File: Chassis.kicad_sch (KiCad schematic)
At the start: 4 parts

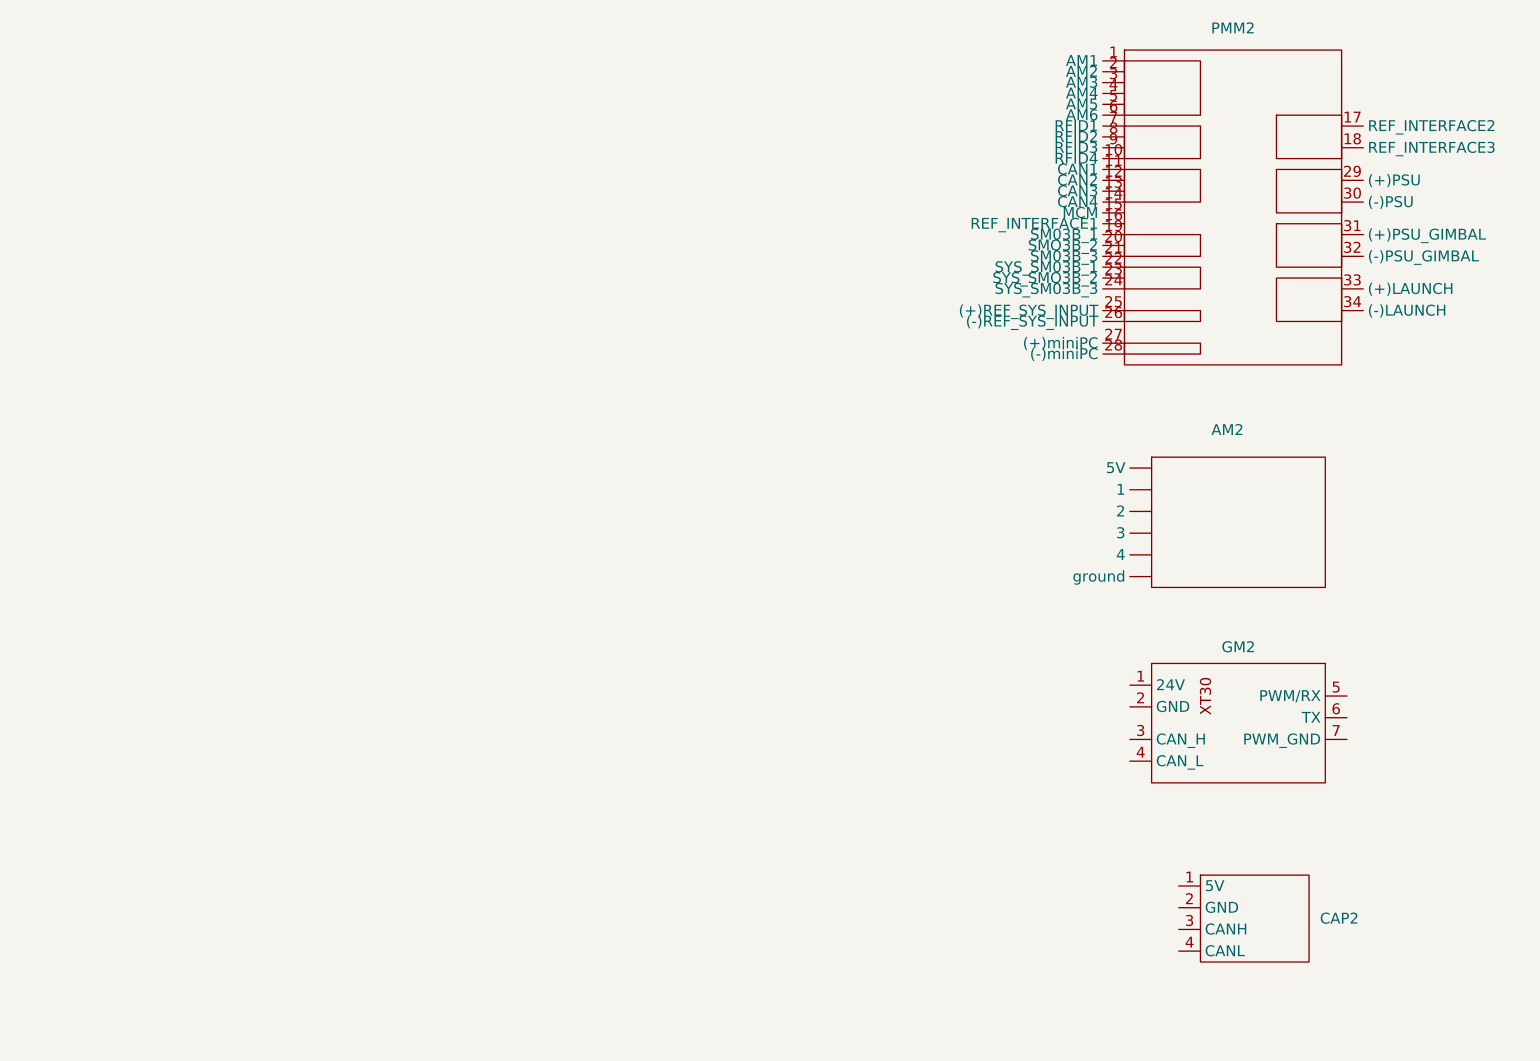
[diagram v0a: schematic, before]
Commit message: Added all connectors + assigned footprints + created PCB file
Starting layout now
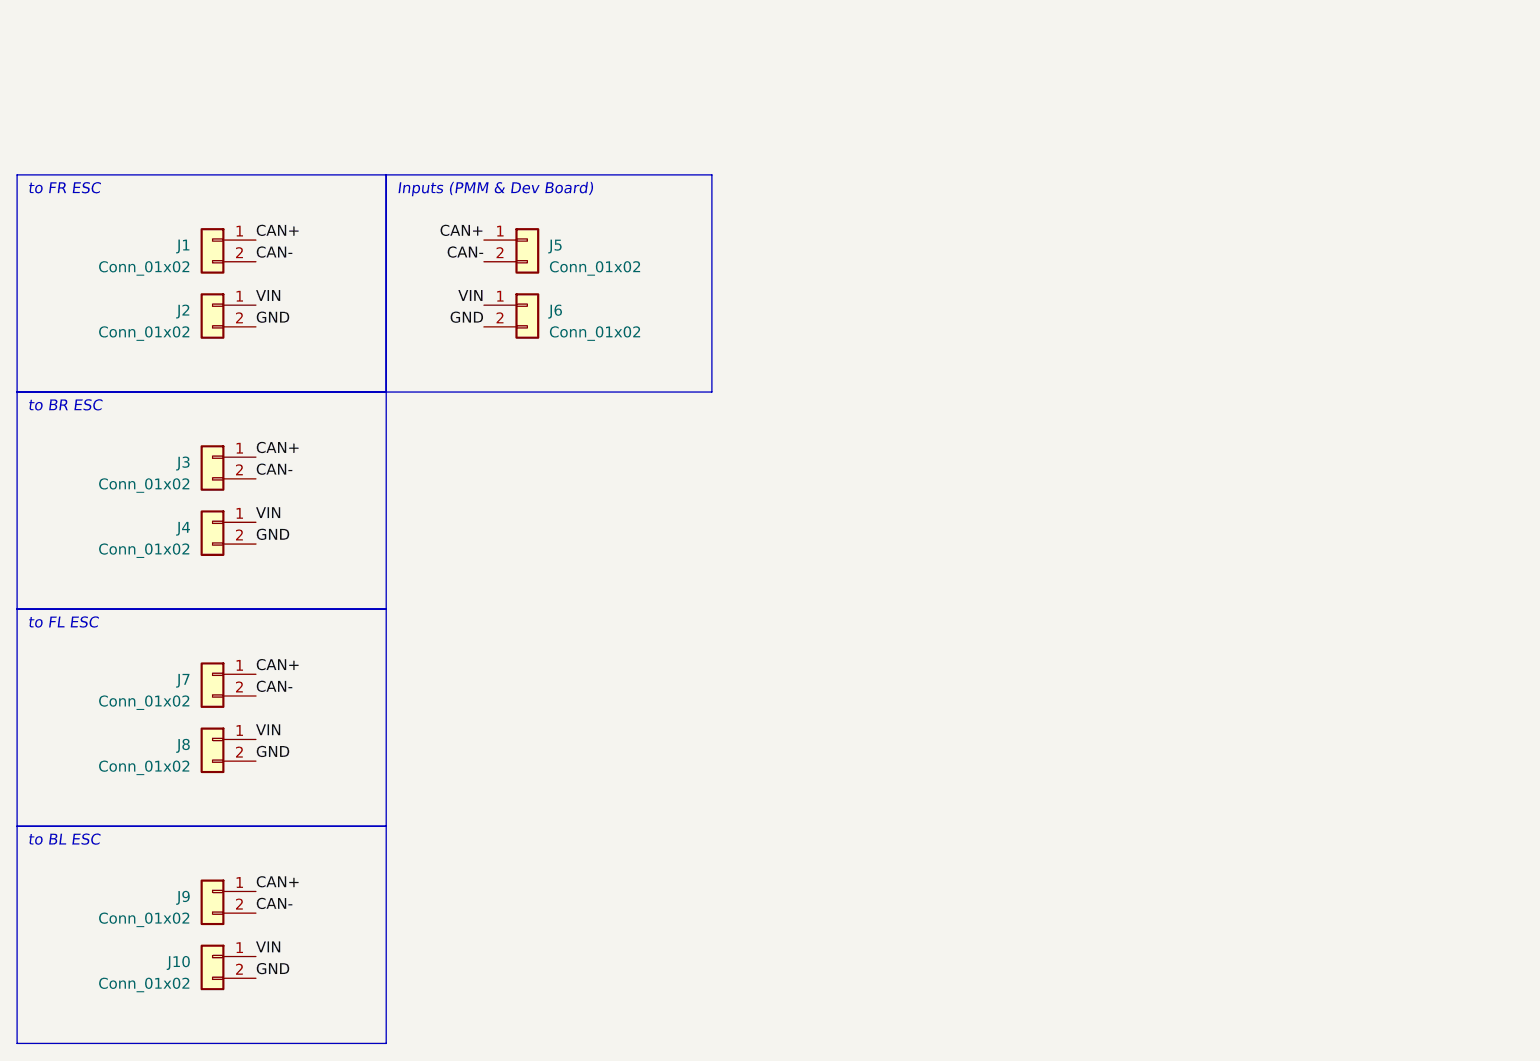
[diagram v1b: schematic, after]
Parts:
- removed AM2: ~, symbol Robomaster_Library:AM
- removed CAP2: ~, symbol Robomaster_Library:CAP
- removed GM2: ~, symbol Robomaster_Library:GM6020
- removed PMM2: ~, symbol Robomaster_Library:PMM
- added J1, J3, J5, J7, J9: Conn_01x02, Connector_JST:JST_GH_BM02B-GHS-TBT_1x02-1MP_P1.25mm_Vertical, symbol Connector_Generic:Conn_01x02
- added J10, J2, J4, J8: Conn_01x02, Connector_AMASS:AMASS_XT30U-F_1x02_P5.0mm_Vertical, symbol Connector_Generic:Conn_01x02
- added J6: Conn_01x02, Connector_AMASS:AMASS_XT60-F_1x02_P7.20mm_Vertical, symbol Connector_Generic:Conn_01x02
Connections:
- new net CAN+: J1.1 (Pin_1), J3.1 (Pin_1), J5.1 (Pin_1), J7.1 (Pin_1), J9.1 (Pin_1)
- new net CAN-: J1.2 (Pin_2), J3.2 (Pin_2), J5.2 (Pin_2), J7.2 (Pin_2), J9.2 (Pin_2)
- new net GND: J10.2 (Pin_2), J2.2 (Pin_2), J4.2 (Pin_2), J6.2 (Pin_2), J8.2 (Pin_2)
- new net VIN: J10.1 (Pin_1), J2.1 (Pin_1), J4.1 (Pin_1), J6.1 (Pin_1), J8.1 (Pin_1)
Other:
- note added: "Inputs (PMM & Dev Board)"
- note added: "to BL ESC"
- note added: "to BR ESC"
- note added: "to FL ESC"
- note added: "to FR ESC"

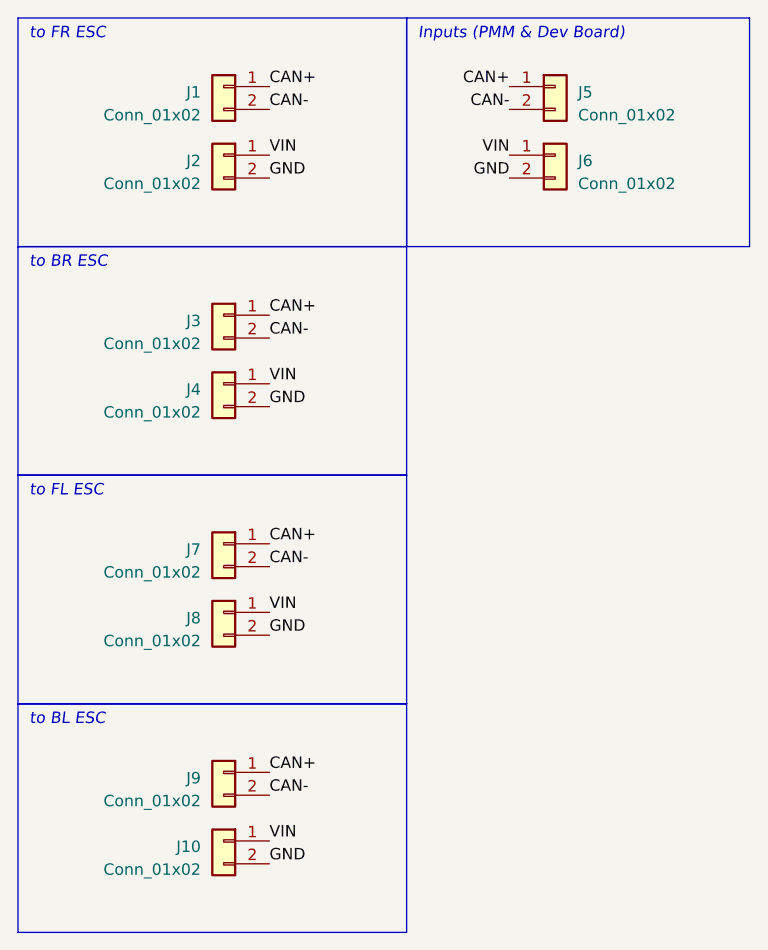
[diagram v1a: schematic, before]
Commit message: Change polarity of pins + add circular trace
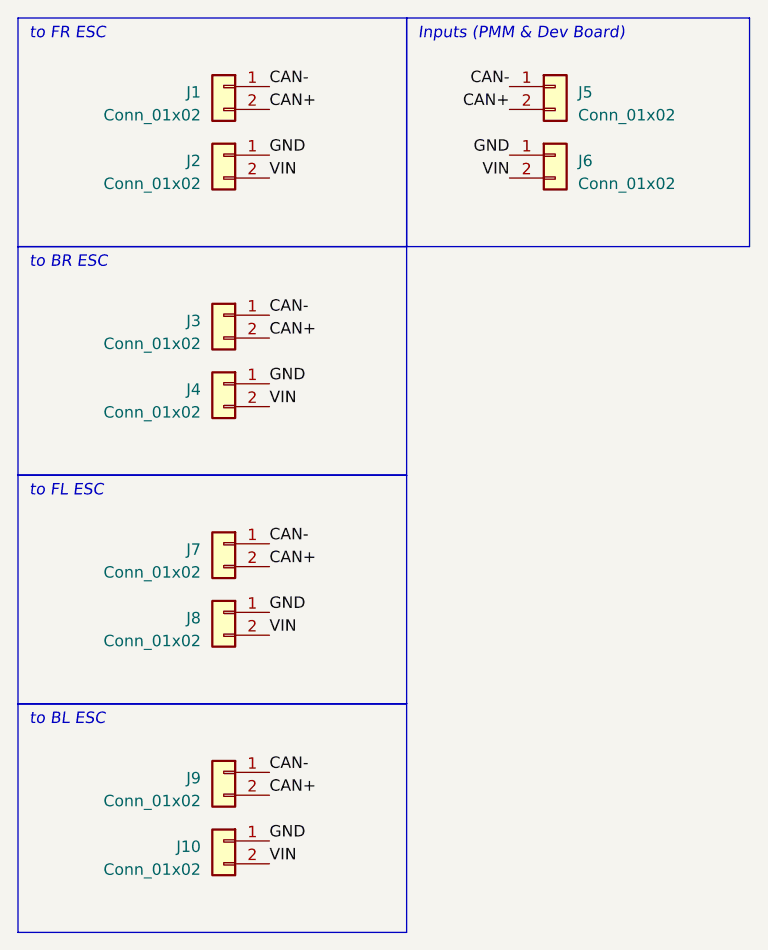
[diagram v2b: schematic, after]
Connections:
- net CAN+: now also J1.2 (Pin_2), J3.2 (Pin_2), J5.2 (Pin_2), J7.2 (Pin_2), J9.2 (Pin_2); no longer J1.1 (Pin_1), J3.1 (Pin_1), J5.1 (Pin_1), J7.1 (Pin_1), J9.1 (Pin_1)
- net CAN-: now also J1.1 (Pin_1), J3.1 (Pin_1), J5.1 (Pin_1), J7.1 (Pin_1), J9.1 (Pin_1); no longer J1.2 (Pin_2), J3.2 (Pin_2), J5.2 (Pin_2), J7.2 (Pin_2), J9.2 (Pin_2)
- net GND: now also J10.1 (Pin_1), J2.1 (Pin_1), J4.1 (Pin_1), J6.1 (Pin_1), J8.1 (Pin_1); no longer J10.2 (Pin_2), J2.2 (Pin_2), J4.2 (Pin_2), J6.2 (Pin_2), J8.2 (Pin_2)
- net VIN: now also J10.2 (Pin_2), J2.2 (Pin_2), J4.2 (Pin_2), J6.2 (Pin_2), J8.2 (Pin_2); no longer J10.1 (Pin_1), J2.1 (Pin_1), J4.1 (Pin_1), J6.1 (Pin_1), J8.1 (Pin_1)
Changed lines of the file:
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@@
     (effects (font (size 1.27 1.27) italic) (justify left bottom))
   )
-  (label "CAN-" (at 133.35 118.11 0) (fields_autoplaced)
+  (label "CAN-" (at 133.35 140.97 0) (fields_autoplaced)
     (effects (font (size 1.27 1.27)) (justify left bottom))
   )
-  (label "VIN" (at 133.35 148.59 0) (fields_autoplaced)
+  (label "GND" (at 160.02 72.39 180) (fields_autoplaced)
+    (effects (font (size 1.27 1.27)) (justify right bottom))
+  )
+  (label "CAN-" (at 133.35 115.57 0) (fields_autoplaced)
     (effects (font (size 1.27 1.27)) (justify left bottom))
   )
-  (label "CAN-" (at 133.35 67.31 0) (fields_autoplaced)
+  (label "CAN+" (at 133.35 118.11 0) (fields_autoplaced)
     (effects (font (size 1.27 1.27)) (justify left bottom))
   )
-  (label "CAN-" (at 133.35 143.51 0) (fields_autoplaced)
+  (label "CAN+" (at 133.35 143.51 0) (fields_autoplaced)
     (effects (font (size 1.27 1.27)) (justify left bottom))
   )
-  (label "VIN" (at 133.35 123.19 0) (fields_autoplaced)
+  (label "CAN-" (at 133.35 90.17 0) (fields_autoplaced)
     (effects (font (size 1.27 1.27)) (justify left bottom))
   )
-  (label "CAN+" (at 160.02 64.77 180) (fields_autoplaced)
+  (label "VIN" (at 133.35 100.33 0) (fields_autoplaced)
+    (effects (font (size 1.27 1.27)) (justify left bottom))
+  )
+  (label "GND" (at 133.35 72.39 0) (fields_autoplaced)
+    (effects (font (size 1.27 1.27)) (justify left bottom))
+  )
+  (label "VIN" (at 133.35 151.13 0) (fields_autoplaced)
+    (effects (font (size 1.27 1.27)) (justify left bottom))
+  )
+  (label "CAN+" (at 133.35 92.71 0) (fields_autoplaced)
+    (effects (font (size 1.27 1.27)) (justify left bottom))
+  )
+  (label "VIN" (at 133.35 125.73 0) (fields_autoplaced)
+    (effects (font (size 1.27 1.27)) (justify left bottom))
+  )
+  (label "VIN" (at 133.35 74.93 0) (fields_autoplaced)
+    (effects (font (size 1.27 1.27)) (justify left bottom))
+  )
+  (label "CAN-" (at 133.35 64.77 0) (fields_autoplaced)
+    (effects (font (size 1.27 1.27)) (justify left bottom))
+  )
+  (label "GND" (at 133.35 123.19 0) (fields_autoplaced)
+    (effects (font (size 1.27 1.27)) (justify left bottom))
+  )
+  (label "CAN+" (at 160.02 67.31 180) (fields_autoplaced)
     (effects (font (size 1.27 1.27)) (justify right bottom))
   )
-  (label "VIN" (at 160.02 72.39 180) (fields_autoplaced)
+  (label "GND" (at 133.35 148.59 0) (fields_autoplaced)
+    (effects (font (size 1.27 1.27)) (justify left bottom))
+  )
+  (label "CAN+" (at 133.35 67.31 0) (fields_autoplaced)
+    (effects (font (size 1.27 1.27)) (justify left bottom))
+  )
+  (label "VIN" (at 160.02 74.93 180) (fields_autoplaced)
     (effects (font (size 1.27 1.27)) (justify right bottom))
   )
-  (label "CAN+" (at 133.35 64.77 0) (fields_autoplaced)
+  (label "GND" (at 133.35 97.79 0) (fields_autoplaced)
     (effects (font (size 1.27 1.27)) (justify left bottom))
   )
-  (label "GND" (at 133.35 74.93 0) (fields_autoplaced)
-    (effects (font (size 1.27 1.27)) (justify left bottom))
-  )
-  (label "VIN" (at 133.35 97.79 0) (fields_autoplaced)
-    (effects (font (size 1.27 1.27)) (justify left bottom))
-  )
-  (label "GND" (at 133.35 151.13 0) (fields_autoplaced)
-    (effects (font (size 1.27 1.27)) (justify left bottom))
-  )
-  (label "CAN+" (at 133.35 115.57 0) (fields_autoplaced)
-    (effects (font (size 1.27 1.27)) (justify left bottom))
-  )
-  (label "CAN-" (at 160.02 67.31 180) (fields_autoplaced)
+  (label "CAN-" (at 160.02 64.77 180) (fields_autoplaced)
     (effects (font (size 1.27 1.27)) (justify right bottom))
   )
-  (label "CAN+" (at 133.35 140.97 0) (fields_autoplaced)
-    (effects (font (size 1.27 1.27)) (justify left bottom))
-  )
-  (label "VIN" (at 133.35 72.39 0) (fields_autoplaced)
-    (effects (font (size 1.27 1.27)) (justify left bottom))
-  )
-  (label "CAN-" (at 133.35 92.71 0) (fields_autoplaced)
-    (effects (font (size 1.27 1.27)) (justify left bottom))
-  )
-  (label "GND" (at 133.35 100.33 0) (fields_autoplaced)
-    (effects (font (size 1.27 1.27)) (justify left bottom))
-  )
-  (label "CAN+" (at 133.35 90.17 0) (fields_autoplaced)
-    (effects (font (size 1.27 1.27)) (justify left bottom))
-  )
-  (label "GND" (at 133.35 125.73 0) (fields_autoplaced)
-    (effects (font (size 1.27 1.27)) (justify left bottom))
-  )
-  (label "GND" (at 160.02 74.93 180) (fields_autoplaced)
-    (effects (font (size 1.27 1.27)) (justify right bottom))
-  )

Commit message: Possible indicator method?
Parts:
- added D1: LED, symbol Device:LED
- added Q1: NMOS, symbol Simulation_SPICE:NMOS
- added R2: REF_R, Resistor_SMD:R_0603_1608Metric_Pad0.98x0.95mm_HandSolder, symbol Device:R_US
- added R3: PUR, Resistor_SMD:R_0603_1608Metric_Pad0.98x0.95mm_HandSolder, symbol Device:R_US
- added TP1, TP2, TP3: TestPoint, TestPoint:TestPoint_Pad_1.0x1.0mm, symbol Connector:TestPoint
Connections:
- net CAN+: now also Q1.2 (G), TP2.1
- net CAN-: now also TP1.1
- net GND: now also R3.2, TP3.1
- net VIN: now also D1.2 (A), R2.1
- new net: D1.1 (K), Q1.1 (D)
- new net VREF: Q1.3 (S), R2.2, R3.1
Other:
- note added: "CAN Indicator Light"
- note added: "Test points"
- moved on the sheet: J5, J6

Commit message: Lakshay's method
I disagree
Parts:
- removed Q1: NMOS, symbol Simulation_SPICE:NMOS
- removed R2: REF_R, Resistor_SMD:R_0603_1608Metric_Pad0.98x0.95mm_HandSolder, symbol Device:R_US
- removed R3: PUR, Resistor_SMD:R_0603_1608Metric_Pad0.98x0.95mm_HandSolder, symbol Device:R_US
- added R1: UR, Resistor_SMD:R_0603_1608Metric_Pad0.98x0.95mm_HandSolder, symbol Device:R_US
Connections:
- net CAN+: now also D1.2 (A)
- net GND: now also R1.1
- net VIN: no longer D1.2 (A)
- net at D1.1 (K): now also R1.2
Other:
- note added: "Lakshay says yes I say no"

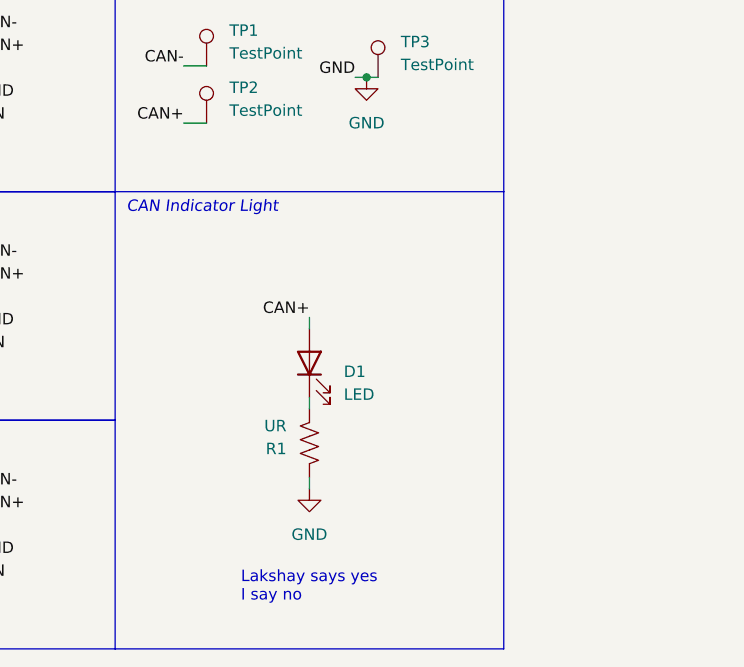
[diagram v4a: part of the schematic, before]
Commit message: Change to MOSFET architecture
Low-side switching ftw
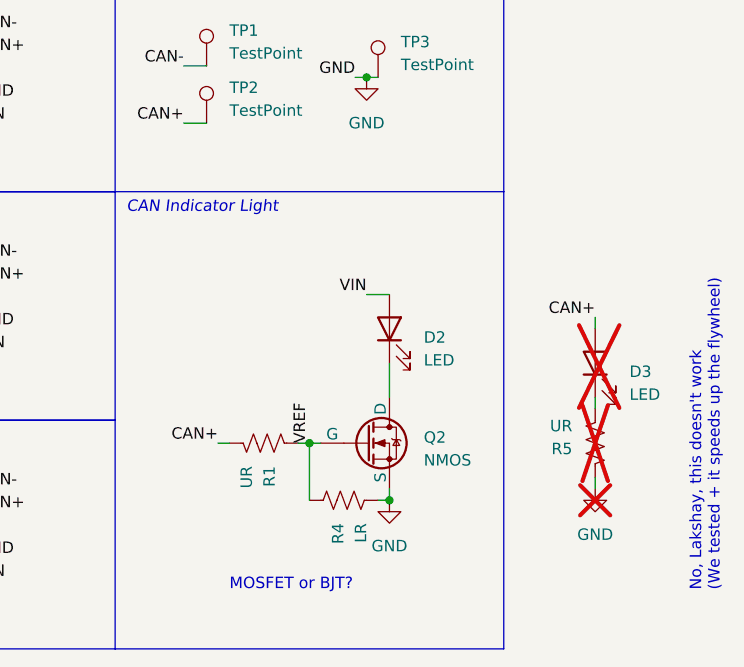
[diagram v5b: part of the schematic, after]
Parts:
- removed D1: LED, symbol Device:LED
- added D2, D3: LED, symbol Device:LED
- added Q2: NMOS, symbol Simulation_SPICE:NMOS
- added R4: LR, Resistor_SMD:R_0603_1608Metric_Pad0.98x0.95mm_HandSolder, symbol Device:R_US
- added R5: UR, Resistor_SMD:R_0603_1608Metric_Pad0.98x0.95mm_HandSolder, symbol Device:R_US
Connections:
- net CAN+: now also R1.2, D3.2 (A)
- net GND: now also Q2.3 (S), R4.2, R5.1; no longer R1.1
- net VIN: now also D2.2 (A)
- new net: D3.1 (K), R5.2
- new net: D2.1 (K), Q2.1 (D)
- new net VREF: Q2.2 (G), R1.1, R4.1
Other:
- note added: "MOSFET or BJT?"
- note added: "No, Lakshay, this doesn't work (We tested + it speeds up the flywheel)"
- note removed: "Lakshay says yes I say no"

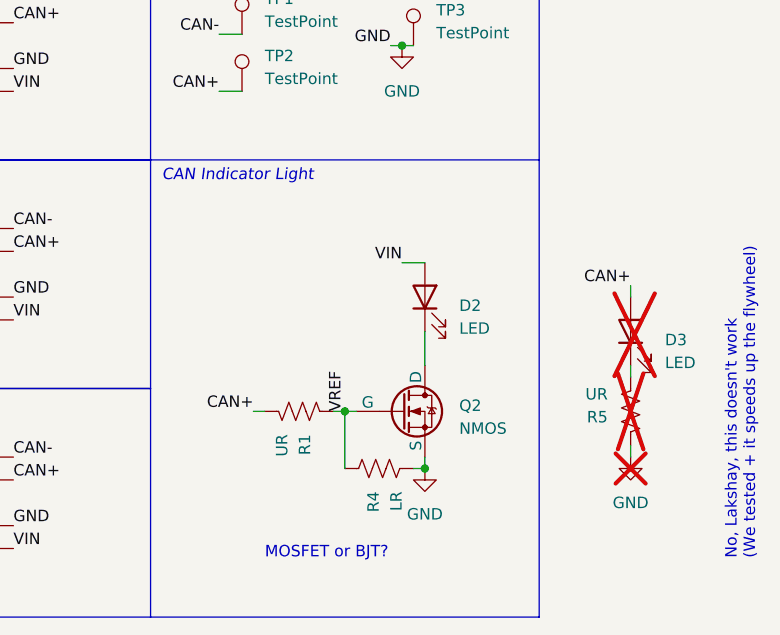
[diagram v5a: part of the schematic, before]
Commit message: Added Resistor and LED footprints to schematic
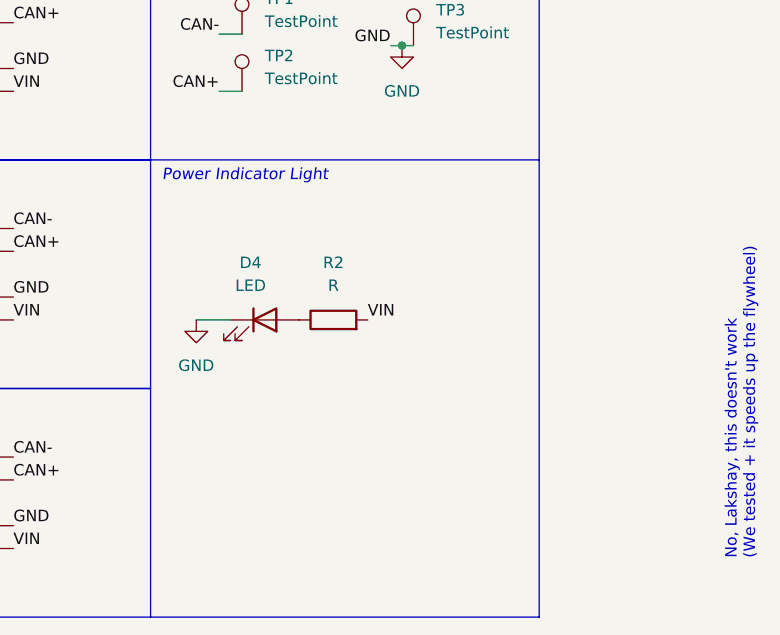
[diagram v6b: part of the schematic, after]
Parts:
- removed D2, D3: LED, symbol Device:LED
- removed Q2: NMOS, symbol Simulation_SPICE:NMOS
- removed R1, R5: UR, Resistor_SMD:R_0603_1608Metric_Pad0.98x0.95mm_HandSolder, symbol Device:R_US
- removed R4: LR, Resistor_SMD:R_0603_1608Metric_Pad0.98x0.95mm_HandSolder, symbol Device:R_US
- added D4: LED, LED_SMD:LED_0603_1608Metric_Pad1.05x0.95mm_HandSolder, symbol Device:LED
- added R2: R, Resistor_SMD:R_0603_1608Metric_Pad0.98x0.95mm_HandSolder, symbol Device:R
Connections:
- net GND: now also D4.1 (K)
- net VIN: now also R2.2
- new net: D4.2 (A), R2.1
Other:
- note added: "Power Indicator Light"
- note removed: "CAN Indicator Light"
- note removed: "MOSFET or BJT?"
